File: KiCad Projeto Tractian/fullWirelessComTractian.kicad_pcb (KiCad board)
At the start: 2 copper layers, 36 parts, among them SW1 ResetButton, U1 ESP8266EX, U2 ATmega328P-A, U3 TXB0108DQSR, U4 MX25R3235FM2xx1, U5 AMS1117-3.3, U6 AMS1117-5.0, X1 ECS-2520MV-xxx-xx, Y1 16MHz, Y2 XTAL 16Mhz ±10ppm (TSX -3225 )

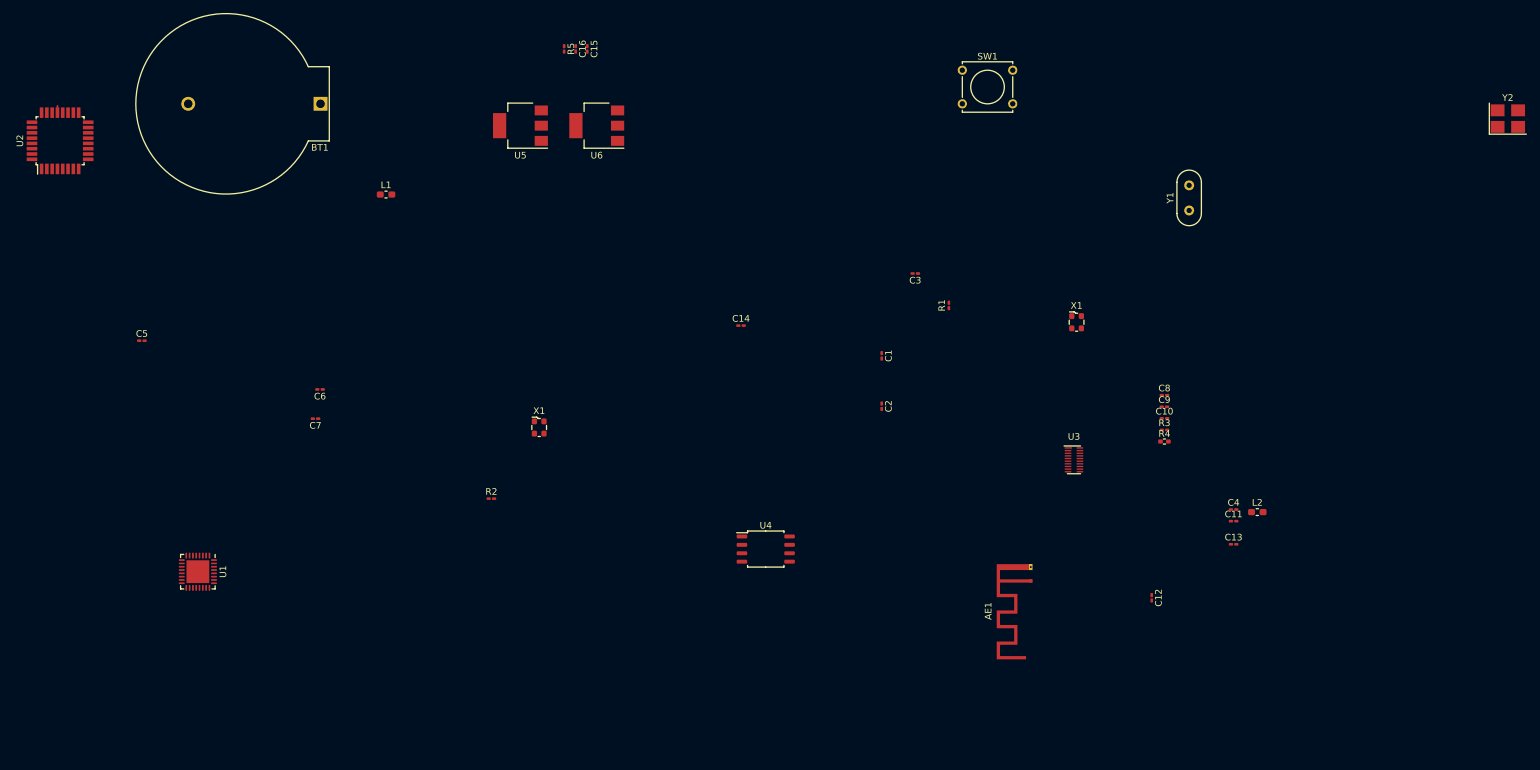
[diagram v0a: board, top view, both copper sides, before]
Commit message: 1 - :fire: | 2 -:memo: | 1 - Remocao dos circuitos p/ Atmega328P-A e Alimentacao Rede | 2 - Add Data Sheet AMS1117
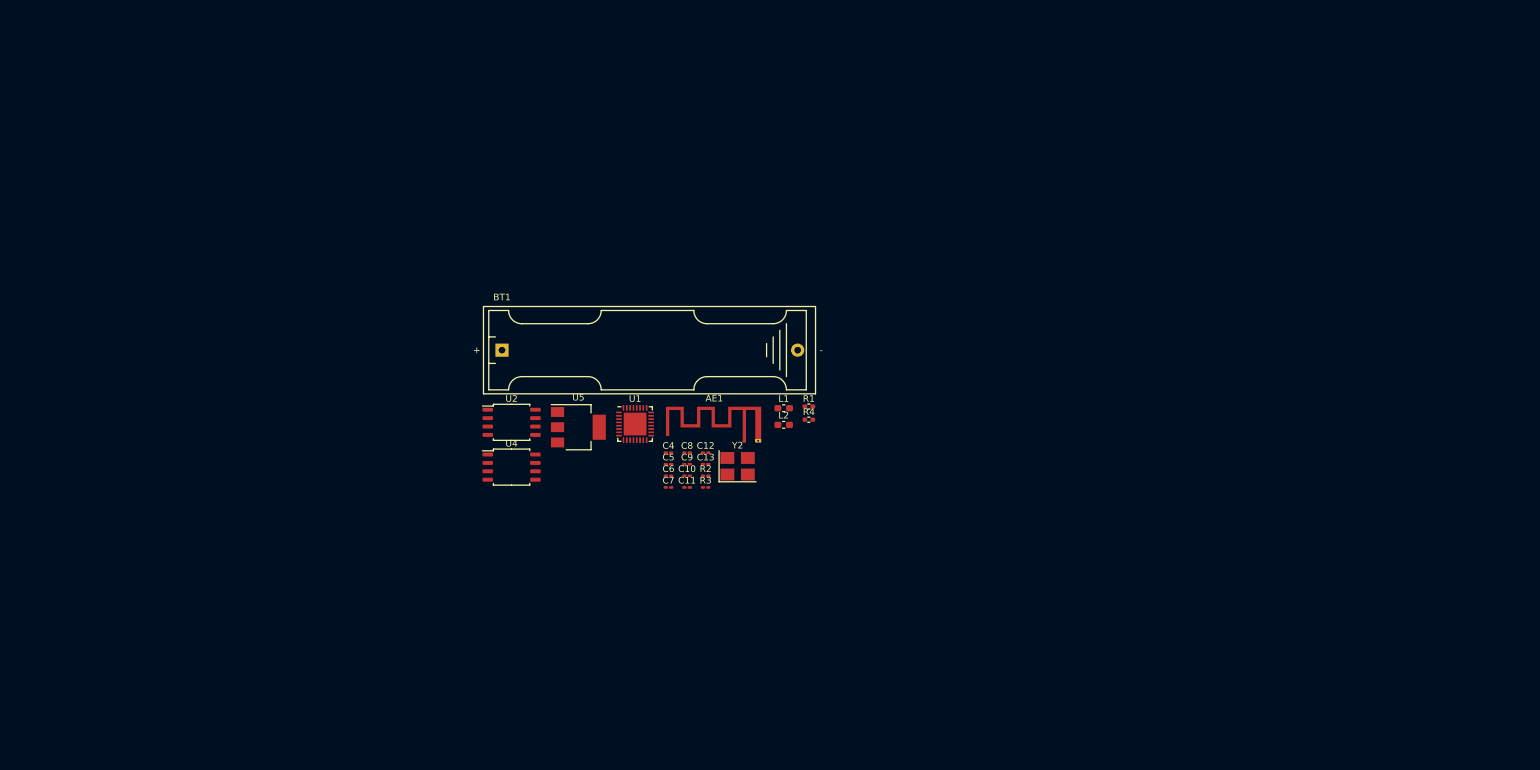
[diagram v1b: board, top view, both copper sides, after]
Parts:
- removed C1: 22pF, Capacitor_SMD:C_0201_0603Metric_Pad0.64x0.40mm_HandSolder
- removed C14: 1uF, Capacitor_SMD:C_0201_0603Metric_Pad0.64x0.40mm_HandSolder
- removed C15, C16: 0.1uF, Capacitor_SMD:C_0201_0603Metric_Pad0.64x0.40mm_HandSolder
- removed C2: 22pf, Capacitor_SMD:C_0201_0603Metric_Pad0.64x0.40mm_HandSolder
- removed C3: 100nF, Capacitor_SMD:C_0201_0603Metric_Pad0.64x0.40mm_HandSolder
- removed R5: 100kΩ, Resistor_SMD:R_0201_0603Metric_Pad0.64x0.40mm_HandSolder
- removed SW1: ResetButton, Button_Switch_THT:SW_Tactile_Straight_KSA0Axx1LFTR
- removed U3: TXB0108DQSR, Package_SON:USON-20_2x4mm_P0.4mm
- removed U6: AMS1117-5.0, Package_TO_SOT_SMD:SOT-223-3_TabPin2
- removed X1 (x2): ECS-2520MV-xxx-xx, Oscillator:Oscillator_SMD_ECS_2520MV-xxx-xx-4Pin_2.5x2.0mm
- removed Y1: 16MHz, Crystal:Crystal_HC52-6mm_Vertical
- BT1: value Battery_Cell -> 1x 3.7V; footprint Battery:BatteryHolder_ComfortableElectronic_CH273-2450_1x2450 -> Battery:BatteryHolder_Keystone_2466_1xAAA
- R1: value 10kΩ -> 200Ω; footprint Resistor_SMD:R_0201_0603Metric_Pad0.64x0.40mm_HandSolder -> Resistor_SMD:R_0402_1005Metric_Pad0.72x0.64mm_HandSolder
- U2: value ATmega328P-A -> MX25R3235FM2xx1; footprint Package_QFP:TQFP-32_7x7mm_P0.8mm -> Package_SO:SOP-8_5.28x5.23mm_P1.27mm
- moved Y2 127.8 mm to (133.2, 80.2)
- moved C4 85.9 mm to (122.7, 78.1)
- moved C11 82.8 mm to (125.5, 83.4)
- moved C5 81.8 mm to (122.7, 79.9)
- moved C13 80.7 mm to (128.3, 79.9)
- moved U2 80.4 mm to (99.0, 73.6), turned to 0 degrees
- moved L2 72.8 mm to (140.1, 73.9)
- moved C10 72.7 mm to (125.5, 81.6)
- moved C8 72.7 mm to (125.5, 78.1)
- moved C9 72.7 mm to (125.5, 79.9)
- moved C12 70.9 mm to (128.3, 78.1), turned to 0 degrees
- moved R3 69.9 mm to (128.3, 83.4)
- moved U1 69.8 mm to (117.7, 73.8), turned to 0 degrees
- moved L1 68.2 mm to (140.1, 71.4)
- moved C7 54.4 mm to (122.7, 83.4), turned to 0 degrees
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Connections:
- R1 pad 1: VCC -> Net-(U1-MTMS)
- R1 pad 2: Net-(U2-~{RESET}/PC6) -> Net-(U2-SCLK)
- U1 pad 10: unconnected-(U1-MTDI-Pad10) -> Net-(U1-MTDI)
- U1 pad 9: unconnected-(U1-MTMS-Pad9) -> Net-(U1-MTMS)
- U2 pad 1: Net-(U2-PD3) -> Net-(U1-MTDO)
- U2 pad 2: unconnected-(U2-PD4-Pad2) -> Net-(U1-MTDI)
- U2 pad 3: GND -> Net-(U1-GPIO0)
- U2 pad 4: Net-(U6-VO) -> GND
- U2 pad 5: GND -> Net-(U1-MTCK)
- U2 pad 6: Net-(U6-VO) -> Net-(U2-SCLK)
- U2 pad 7: Net-(U2-XTAL1/PB6) -> Net-(U1-GPIO2)
- U2 pad 8: Net-(U2-XTAL2/PB7) -> Net-(U1-VDDD)
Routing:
- net GND: track 1.05 -> 0.00 mm

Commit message: :arrow_up: Modificacao da PCB para 4-layers
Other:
- copper layers 2 -> 4
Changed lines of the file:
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@@
   (paper "A4")
   (layers
-    (0 "F.Cu" signal)
-    (31 "B.Cu" signal)
+    (0 "F.Cu" signal "Signal & Components")
+    (1 "In1.Cu" power "GND")
+    (2 "In2.Cu" power "Power")
+    (31 "B.Cu" signal "Signal Only")
     (32 "B.Adhes" user "B.Adhesive")
     (33 "F.Adhes" user "F.Adhesive")
@@
       (layer "F.Mask" (type "Top Solder Mask") (thickness 0.01))
       (layer "F.Cu" (type "copper") (thickness 0.035))
-      (layer "dielectric 1" (type "core") (thickness 1.51) (material "FR4") (epsilon_r 4.5) (loss_tangent 0.02))
+      (layer "dielectric 1" (type "prepreg") (thickness 0.1) (material "FR4") (epsilon_r 4.5) (loss_tangent 0.02))
+      (layer "In1.Cu" (type "copper") (thickness 0.035))
+      (layer "dielectric 2" (type "core") (thickness 1.24) (material "FR4") (epsilon_r 4.5) (loss_tangent 0.02))
+      (layer "In2.Cu" (type "copper") (thickness 0.035))
+      (layer "dielectric 3" (type "prepreg") (thickness 0.1) (material "FR4") (epsilon_r 4.5) (loss_tangent 0.02))
       (layer "B.Cu" (type "copper") (thickness 0.035))
       (layer "B.Mask" (type "Bottom Solder Mask") (thickness 0.01))

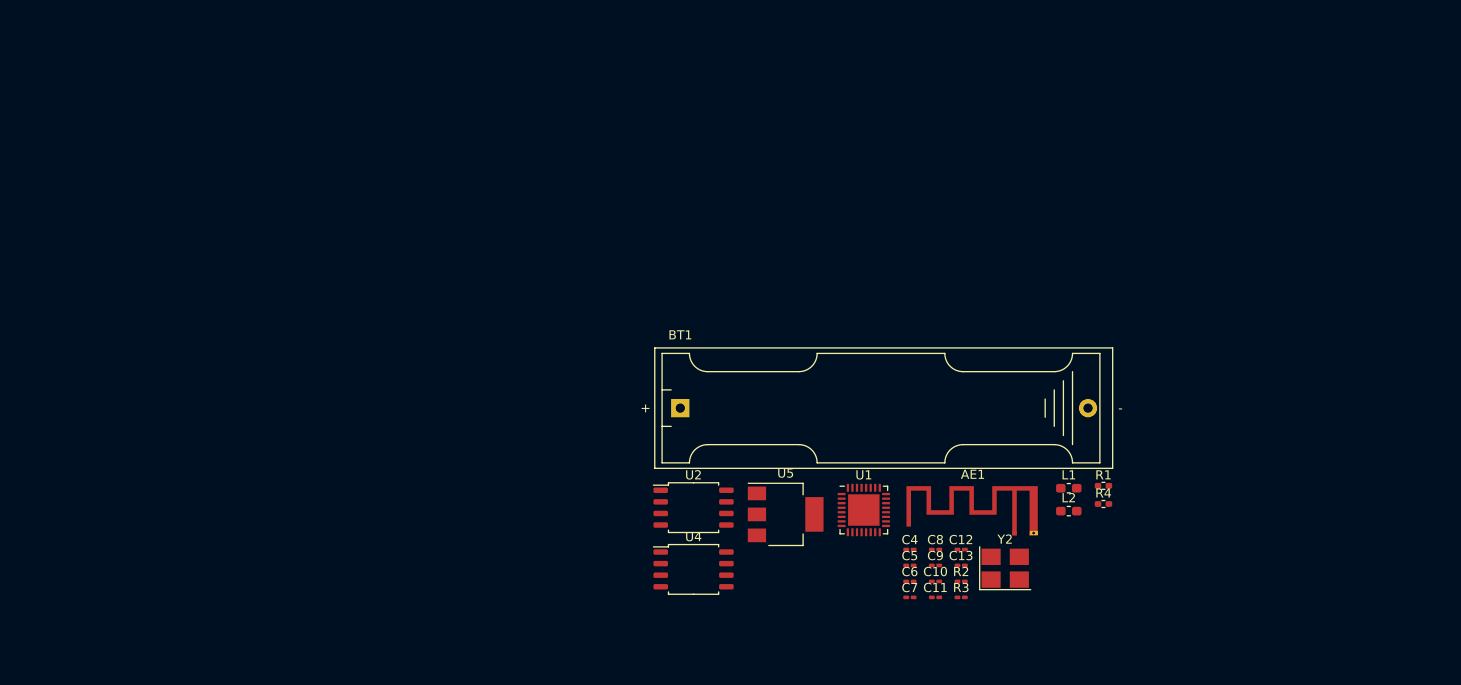
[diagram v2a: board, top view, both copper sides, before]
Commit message: :construction: Add GND Mounting Holes and PCB borders
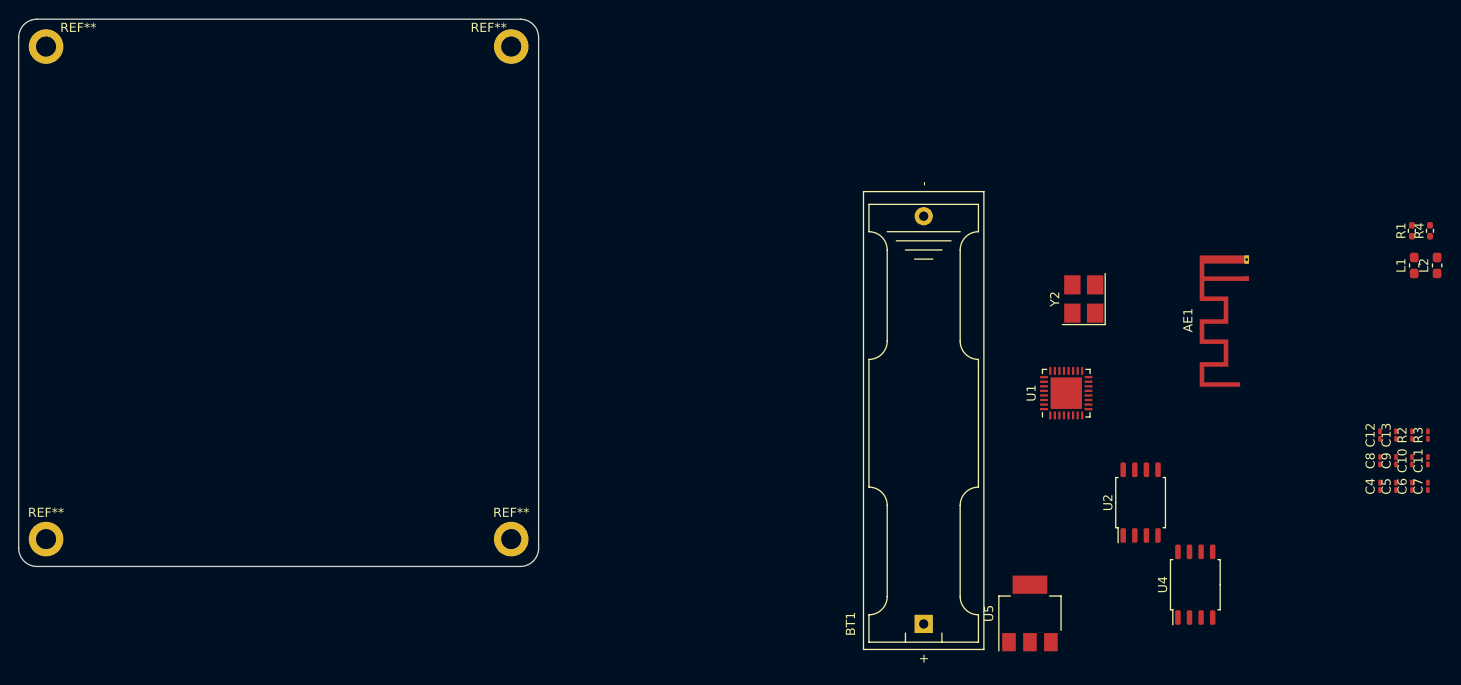
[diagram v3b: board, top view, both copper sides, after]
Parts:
- added REF**: MountingHole_2.2mm_M2_DIN965_Pad, MountingHole:MountingHole_2.2mm_M2_DIN965_Pad, F.Cu at (79.0, 77.0)
- added REF**: MountingHole_2.2mm_M2_DIN965_Pad, MountingHole:MountingHole_2.2mm_M2_DIN965_Pad, F.Cu at (28.0, 77.0)
- added REF**: MountingHole_2.2mm_M2_DIN965_Pad, MountingHole:MountingHole_2.2mm_M2_DIN965_Pad, F.Cu at (28.0, 23.0)
- added REF**: MountingHole_2.2mm_M2_DIN965_Pad, MountingHole:MountingHole_2.2mm_M2_DIN965_Pad, F.Cu at (79.0, 23.0)
- moved C7 58.1 mm to (179.5, 71.2), turned to 90 degrees
- moved C11 56.0 mm to (179.5, 68.4), turned to 90 degrees
- moved C6 56.0 mm to (177.8, 71.2), turned to 90 degrees
- moved U4 55.0 mm to (154.0, 82.0), turned to 90 degrees
- moved R3 54.2 mm to (179.5, 65.6), turned to 90 degrees
- moved C5 54.0 mm to (176.0, 71.2), turned to 90 degrees
- moved C10 53.9 mm to (177.8, 68.4), turned to 90 degrees
- moved C4 52.0 mm to (174.2, 71.2), turned to 90 degrees
- moved R2 52.0 mm to (177.8, 65.6), turned to 90 degrees
- moved C9 51.8 mm to (176.0, 68.4), turned to 90 degrees
- moved C13 49.8 mm to (176.0, 65.6), turned to 90 degrees
- moved C8 49.7 mm to (174.2, 68.4), turned to 90 degrees
- moved U2 49.0 mm to (148.0, 73.0), turned to 90 degrees
- moved L2 48.5 mm to (180.5, 47.0), turned to 90 degrees
- moved C12 47.6 mm to (174.2, 65.6), turned to 90 degrees
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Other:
- board outline added: 57 x 60 mm

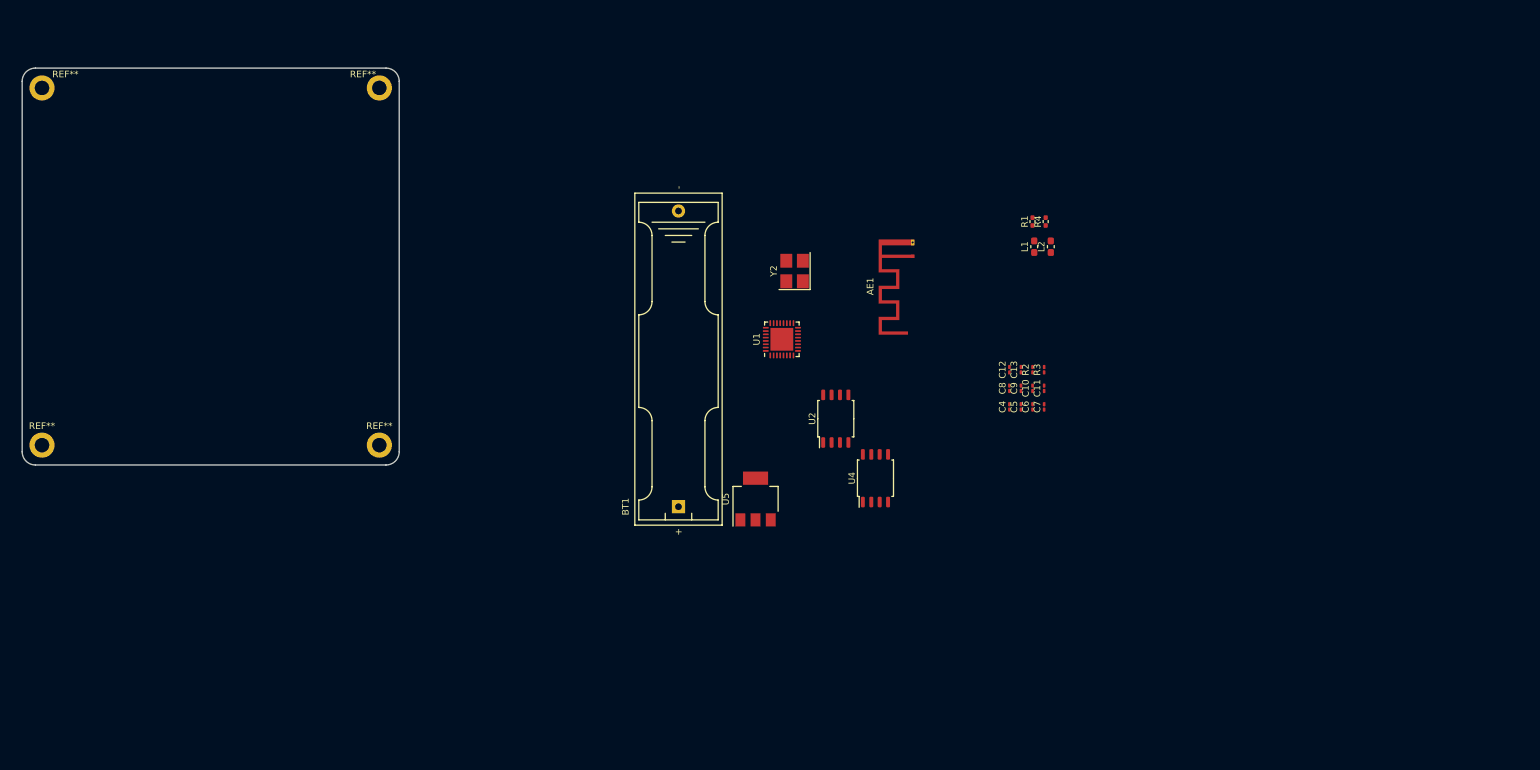
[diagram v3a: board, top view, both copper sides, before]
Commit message: :construction: Arranjo dos componentes | destaque para o circuito pi e XTAL em 0.8mm
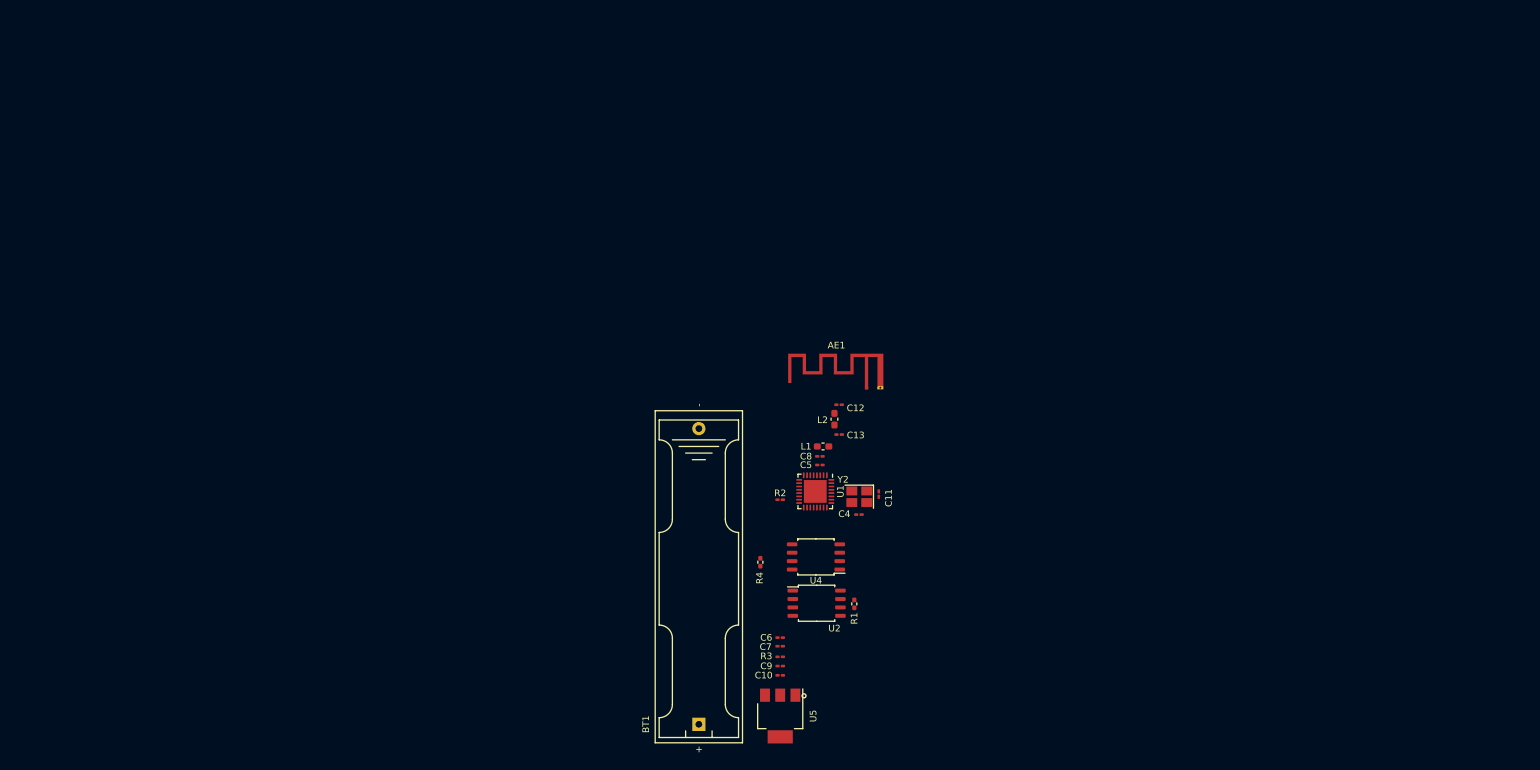
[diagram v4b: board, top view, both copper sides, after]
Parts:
- removed REF** (x4): MountingHole_2.2mm_M2_DIN965_Pad, MountingHole:MountingHole_2.2mm_M2_DIN965_Pad
- Y2: value XTAL 16Mhz ±10ppm (TSX -3225 ) -> XTAL; footprint Oscillator:Oscillator_SMD_SeikoEpson_SG8002CE-4Pin_3.2x2.5mm_HandSoldering -> Oscillator:Oscillator_SMD_SeikoEpson_SG210-4Pin_2.5x2.0mm_HandSoldering
- moved R4 67.2 mm to (136.6, 94.7), turned to -90 degrees
- moved R1 63.8 mm to (150.8, 101.0), turned to -90 degrees
- moved R3 59.0 mm to (139.6, 109.0), turned to 0 degrees
- moved C10 57.8 mm to (139.6, 111.8), turned to 0 degrees
- moved C9 55.6 mm to (139.6, 110.4), turned to 0 degrees
- moved C7 53.9 mm to (139.6, 107.4), turned to 180 degrees
- moved C6 51.7 mm to (139.6, 106.1), turned to 180 degrees
- moved L1 43.9 mm to (146.1, 77.2), turned to 0 degrees
- moved R2 42.9 mm to (139.6, 85.2), turned to 180 degrees
- moved L2 41.8 mm to (147.8, 73.1), turned to -90 degrees
- moved Y2 35.5 mm to (151.6, 84.8), turned to 180 degrees
- moved BT1 33.0 mm to (127.3, 119.2)
- moved U5 33.0 mm to (139.6, 118.0), turned to -90 degrees
- moved C5 31.6 mm to (145.6, 80.0), turned to 180 degrees
- moved C8 30.4 mm to (145.6, 78.7), turned to 180 degrees
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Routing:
- net (no net): vias 0 -> 1
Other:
- board outline removed
